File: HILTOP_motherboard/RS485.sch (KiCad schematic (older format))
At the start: 24 parts, among them U13 CME0303S3C, U14 ADuM1401, U15 ADuM1401, U16 CME0303S3C, U17 ISL83491, U18 ISL83491

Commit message: Added new USB2.0 device
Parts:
- removed R72, R78: 0R, Resistors_SMD:R_0603, symbol R
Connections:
- wire segments 124 -> 116
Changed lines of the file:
@@
 LIBS:regul
 LIBS:references
-LIBS:pspice
 LIBS:Power_Management
 LIBS:powerint
@@
 LIBS:Diode
 LIBS:digital-audio
-LIBS:device
 LIBS:Decawave
 LIBS:dc-dc
@@
 LIBS:adc-dac
 LIBS:ac-dc
+LIBS:device
 LIBS:HILTOP_Motherboard-cache
 EELAYER 25 0
@@
 $Descr A4 11693 8268
 encoding utf-8
-Sheet 4 8
+Sheet 4 9
 Title "HILTOP Motherboard"
 Date "26th January 2018"
@@
 F 4 "131-001" H 1950 6700 60  0001 C CNN "Devtank"
 	1    1950 6700
-	1    0    0    -1
-$EndComp
-$Comp
-L GND_ISO3 #PWR0186
-U 1 1 589A9056
-P 3200 7000
-F 0 "#PWR0186" H 3200 6750 50  0001 C CNN
-F 1 "GND_ISO3" H 3200 6850 50  0000 C CNN
-F 2 "" H 3200 7000 50  0000 C CNN
-F 3 "" H 3200 7000 50  0000 C CNN
-	1    3200 7000
 	1    0    0    -1
 $EndComp
@@
 F 3 "" H 5100 1350 50  0000 C CNN
 	1    5100 1350
-	1    0    0    -1
-$EndComp
-$Comp
-L +3V3_ISO3 #PWR0198
-U 1 1 589A906E
-P 3200 6400
-F 0 "#PWR0198" H 3200 6250 50  0001 C CNN
-F 1 "+3V3_ISO3" H 3200 6540 50  0000 C CNN
-F 2 "" H 3200 6400 50  0000 C CNN
-F 3 "" H 3200 6400 50  0000 C CNN
-	1    3200 6400
 	1    0    0    -1
 $EndComp
@@
 	1    0    0    -1
 $EndComp
-$Comp
-L R R78
-U 1 1 589A947C
-P 4450 3250
-F 0 "R78" V 4530 3250 50  0000 C CNN
-F 1 "0R" V 4450 3250 50  0000 C CNN
-F 2 "Resistors_SMD:R_0603" V 4380 3250 50  0001 C CNN
-F 3 "" H 4450 3250 50  0000 C CNN
-F 4 "101-005" V 4450 3250 60  0001 C CNN "Devtank"
-	1    4450 3250
-	0    1    1    0
-$EndComp
 Wire Wire Line
 	6350 1200 6350 1550
@@
 Wire Wire Line
 	3250 3950 3250 4050
-Wire Wire Line
-	4600 3250 5050 3250
-Wire Wire Line
-	5050 3250 5050 2850
-Connection ~ 5050 2850
-Wire Wire Line
-	4300 3250 3900 3250
-Wire Wire Line
-	3900 3250 3900 2850
-Connection ~ 3900 2850
-Wire Wire Line
-	4600 5700 5050 5700
-Wire Wire Line
-	5050 5700 5050 5300
-Connection ~ 5050 5300
-Wire Wire Line
-	4300 5700 3900 5700
-Wire Wire Line
-	3900 5700 3900 5300
-Connection ~ 3900 5300
 $Comp
 L C C108
@@
 $EndComp
 $Comp
-L R R72
-U 1 1 593A9C0A
-P 4450 5700
-F 0 "R72" V 4530 5700 50  0000 C CNN
-F 1 "0R" V 4450 5700 50  0000 C CNN
-F 2 "Resistors_SMD:R_0603" V 4380 5700 50  0001 C CNN
-F 3 "" H 4450 5700 50  0000 C CNN
-F 4 "101-005" V 4450 5700 60  0001 C CNN "Devtank"
-	1    4450 5700
-	0    1    1    0
-$EndComp
-$Comp
 L C C105
 U 1 1 593AA7E2
@@
 Wire Wire Line
 	1050 6850 1050 7050
+$Comp
+L GND_ISO3 #PWR0186
+U 1 1 589A9056
+P 3200 7000
+F 0 "#PWR0186" H 3200 6750 50  0001 C CNN
+F 1 "GND_ISO3" H 3200 6850 50  0000 C CNN
+F 2 "" H 3200 7000 50  0000 C CNN
+F 3 "" H 3200 7000 50  0000 C CNN
+	1    3200 7000
+	1    0    0    -1
+$EndComp
+$Comp
+L +3V3_ISO3 #PWR0198
+U 1 1 589A906E
+P 3200 6400
+F 0 "#PWR0198" H 3200 6250 50  0001 C CNN
+F 1 "+3V3_ISO3" H 3200 6540 50  0000 C CNN
+F 2 "" H 3200 6400 50  0000 C CNN
+F 3 "" H 3200 6400 50  0000 C CNN
+	1    3200 6400
+	1    0    0    -1
+$EndComp
 $EndSCHEMATC

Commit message: Finished CAN nd RS485 interface circuits
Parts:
- removed C105: 4.7uF, Capacitors_SMD:C_0805, symbol C
- removed C108, C84: 100nF, Capacitors_SMD:C_0603, symbol C
- removed C79: 2.2uF, Capacitors_SMD:C_0805, symbol C
- removed JP1, JP2: Jumper_NO_Small, Pin_Headers:Pin_Header_Straight_1x02_Pitch2.54mm, symbol Jumper_NO_Small
- removed L6: 10uH, KiCAD_PCB_Lib:Inductor_MuRata_82103C, symbol L
- removed R80, R81: 100R, Resistors_SMD:R_0603, symbol R
- removed U14, U15: ADuM1401, Housings_SOIC:SOIC-16W_7.5x10.3mm_Pitch1.27mm, symbol ADuM1401
- removed U16: CME0303S3C, KiCAD_PCB_Lib:CME_XXXX_S3C_PSU_MODULE, symbol CME0303S3C
- removed U17, U18: ISL83491, Housings_SOIC:SOIC-14_3.9x8.7mm_Pitch1.27mm, symbol ISL83491
- added C? (x2): 470pF, Capacitor_SMD:C_0603_1608Metric, symbol C
- added C?: 4.7uF, Capacitors_SMD:C_0805, symbol C
- added C?: 2.2uF, Capacitors_SMD:C_0805, symbol C
- added D? (x4): RED_LED, LED_SMD:LED_0603_1608Metric, symbol LED
- added L?: 15uH, KiCAD_PCB_Lib:Inductor_MuRata_82103C, symbol L
- added R? (x4): 10K, Capacitor_SMD:C_0603_1608Metric, symbol R
- added R? (x4): 1K, Capacitor_SMD:C_0603_1608Metric, symbol R
- added U? (x2): ISO3080, Package_SOIC:SOIC-16W_7.5x10.3mm_P1.27mm, symbol ISO3080
- added U? (x4): USB6B1, Housings_SOIC:SOIC-8_3.9x4.9mm_Pitch1.27mm, symbol USB6B1
- added U?: AM1S-0505SZ, KiCAD_PCB_Lib:CME_XXXX_S3C_PSU_MODULE, symbol CME0303S3C
- L5: value 10uH -> 15uH; Devtank 112-004 -> 112-007
- U13: value CME0303S3C -> AM1S-0505SZ; Devtank 131-001 -> 131-002
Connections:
- net labels added: +5V, +5V_ISO3, +5V_ISO4, RS485_CH1_A, RS485_CH1_B, RS485_CH1_RX_LED, RS485_CH1_TX_LED, RS485_CH1_Y, RS485_CH1_Z, RS485_CH2_A, RS485_CH2_B, RS485_CH2_RX_LED, RS485_CH2_TX_LED, RS485_CH2_Y, RS485_CH2_Z
- net labels removed: +3V3_ISO3, +3V3_ISO4, RS485_CH1_AB_IN_+, RS485_CH1_AB_IN_-, RS485_CH1_YZ_OUT_+, RS485_CH1_YZ_OUT_-, RS485_CH2_AB_IN_+, RS485_CH2_AB_IN_-, RS485_CH2_YZ_OUT_+, RS485_CH2_YZ_OUT_-
- wire segments 116 -> 148
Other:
- note removed: "OPTIONAL: Line Termination\n"
- moved on the sheet: C76, C78, C82, C83, L5, U13

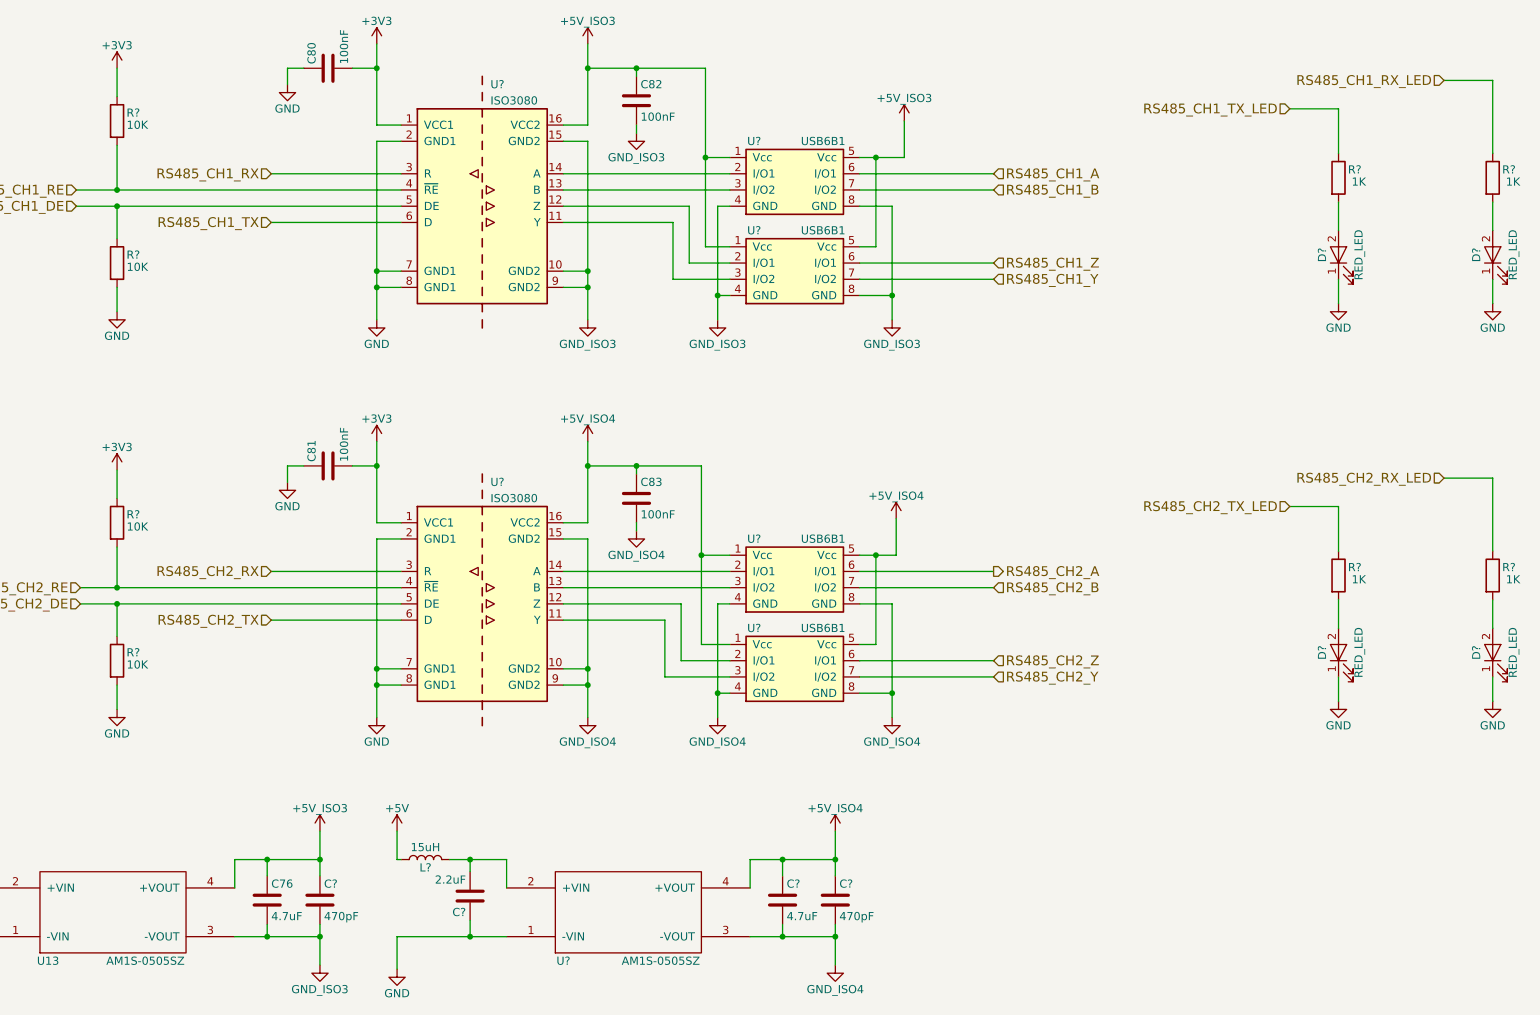
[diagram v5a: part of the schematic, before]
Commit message: Furthe progress on Schematics, assigned all main footprints using latest libraries, removed unwanted tracking and parts from original PCB layout
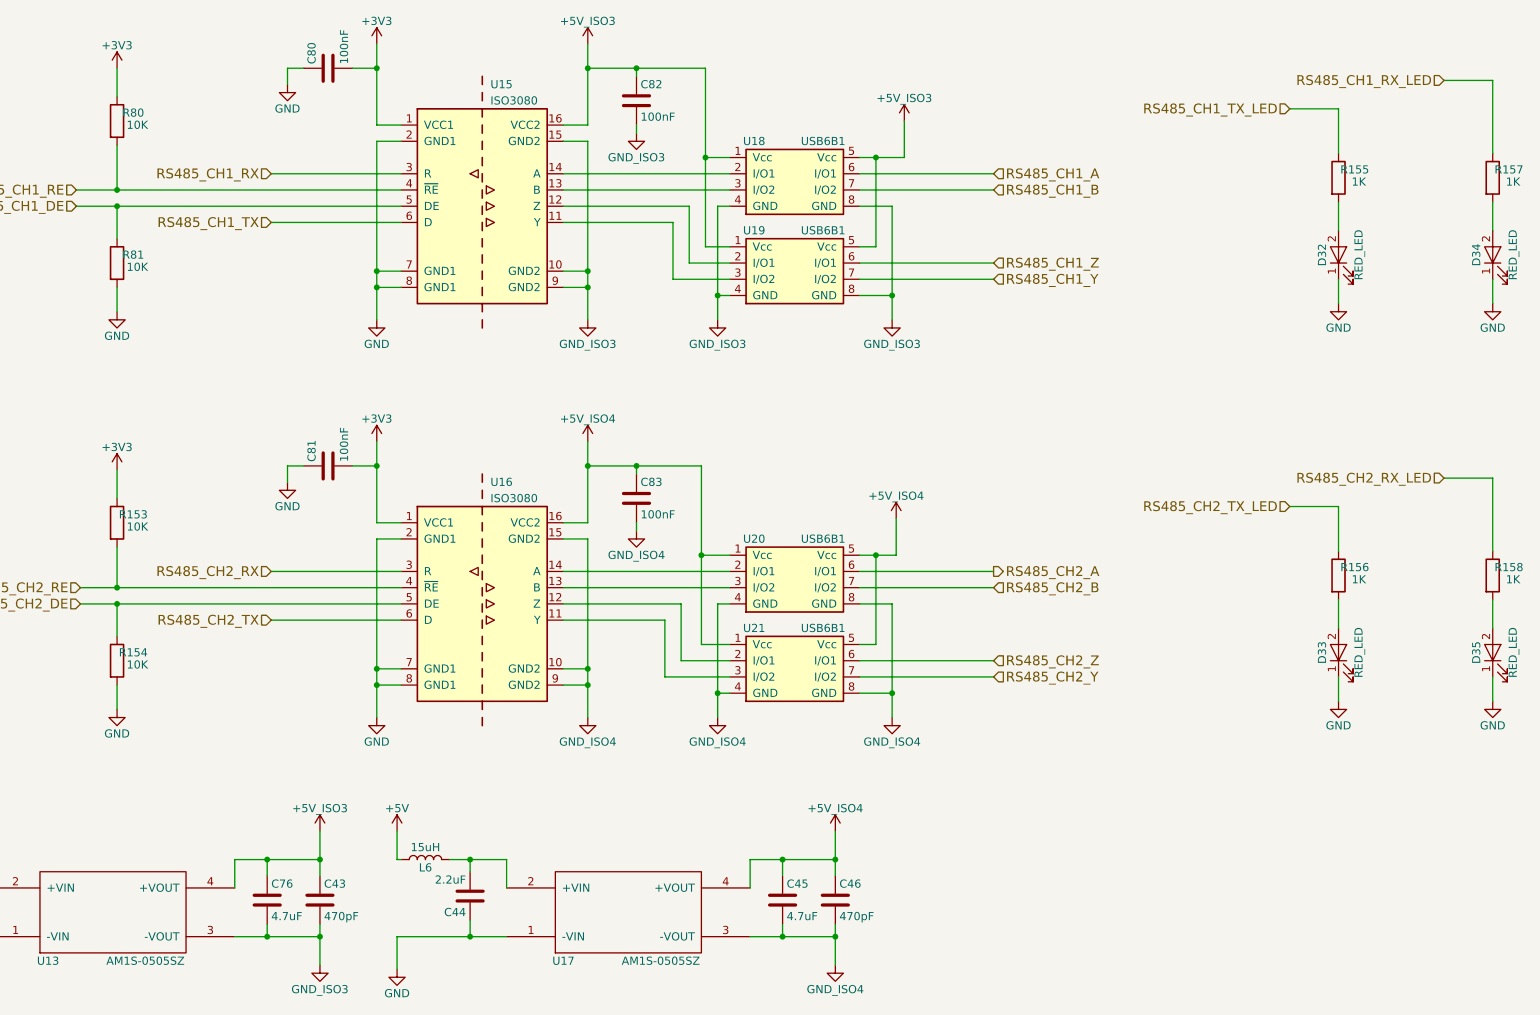
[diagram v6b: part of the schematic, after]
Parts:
- C44, C45: renamed from C?; footprint Capacitors_SMD:C_0805 -> Capacitor_SMD:C_0805_2012Metric
- C76, C78: footprint Capacitors_SMD:C_0805 -> Capacitor_SMD:C_0805_2012Metric
- C80, C81, C82, C83: footprint Capacitors_SMD:C_0603 -> Capacitor_SMD:C_0603_1608Metric
- L5: footprint KiCAD_PCB_Lib:Inductor_MuRata_82103C -> Devtank_PCB_Lib:Inductor_MuRata_82103C
- L6: renamed from L?; footprint KiCAD_PCB_Lib:Inductor_MuRata_82103C -> Devtank_PCB_Lib:Inductor_MuRata_82103C
- R153, R154, R155, R156, R157, R158, R80, R81: renamed from R?; footprint Capacitor_SMD:C_0603_1608Metric -> Resistor_SMD:R_0603_1608Metric
- U13: footprint KiCAD_PCB_Lib:CME_XXXX_S3C_PSU_MODULE -> Devtank_PCB_Lib:CME_XXXX_S3C_PSU_MODULE
- U17: renamed from U?; footprint KiCAD_PCB_Lib:CME_XXXX_S3C_PSU_MODULE -> Devtank_PCB_Lib:CME_XXXX_S3C_PSU_MODULE
- U18, U19, U20, U21: renamed from U?; footprint Housings_SOIC:SOIC-8_3.9x4.9mm_Pitch1.27mm -> Package_SOIC:SOIC-8_3.9x4.9mm_P1.27mm
- gave numbers to parts that had none: 8

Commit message: Schematics complete - 1st draft
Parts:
- removed D32, D33, D34, D35: RED_LED, LED_SMD:LED_0603_1608Metric, symbol LED
- removed R153, R154, R80: 10K, Resistor_SMD:R_0603_1608Metric, symbol R
- removed R155, R156, R157, R158: 1K, Resistor_SMD:R_0603_1608Metric, symbol R
- added C226, C228, C230, C231, C232, C233, C234, C235: 100nF, Capacitor_SMD:C_0603_1608Metric, symbol device:C
- added C227, C229: 1uF, Capacitor_SMD:C_0603_1608Metric, symbol device:C
- added FB10, FB6: 120R_100MHz, Resistor_SMD:R_0603_1608Metric, symbol device:L
- added R221, R222, R244: 10K, Resistor_SMD:R_0603_1608Metric, symbol device:R
- added R223: 0R, Resistor_SMD:R_0603_1608Metric, symbol device:R
- added R243: DNF, Resistor_SMD:R_0603_1608Metric, symbol device:R
- added U43, U44: MAX3107, Package_SO:SSOP-24_5.3x8.2mm_P0.65mm, symbol Devtank:MAX3107
- added Y8, Y9: 3.6864MHz Crystal, Crystal:Crystal_SMD_SeikoEpson_MA505-2Pin_12.7x5.1mm, symbol device:Crystal
- C43, C44, C45, C46, C76, C78, C80, C81, C82, C83: symbol C -> device:C
- L5, L6: symbol L -> device:L
- R81: symbol R -> device:R
- U13, U17: symbol CME0303S3C -> Devtank:CME0303S3C
- U15, U16: symbol ISO3080 -> HILTOP_Motherboard-rescue:ISO3080
- U18, U19, U20, U21: symbol USB6B1 -> ESD_Protection:USB6B1
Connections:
- net RS485_CH1_RE is gone; now on net GND: U15.4 (~RE)
- net RS485_CH2_RE is gone; now on net GND: U16.4 (~RE)
- net +3V3: now also C226.2, C228.2, C232.1, C233.1, C234.1, C235.1, R221.1, R222.1, R243.1, U43.13 (VL), U43.23 (VEXT), U43.5 (~I2C/~SPI), U43.6 (LDOEN), U44.13 (VL), U44.23 (VEXT), U44.5 (~I2C/~SPI), U44.6 (LDOEN)
- net GND: now also C226.1, C227.1, C228.1, C229.1, C230.1, C231.1, C232.2, C233.2, C234.2, C235.2, R244.2, U43.14 (DGND), U43.2 (AGND), U44.14 (DGND), U44.2 (AGND)
- net RS485_CH1_DE: no longer names the net of R81.1, U15.5 (DE)
- net RS485_CH1_DE: now also U43.20 (~RTS~/CLKOUT)
- net RS485_CH1_RX: no longer names the net of U15.3 (R)
- net RS485_CH1_RX: now also U43.21 (RX)
- net RS485_CH1_TX: no longer names the net of U15.6 (D)
- net RS485_CH1_TX: now also U43.22 (TX)
- net RS485_CH2_DE: no longer names the net of U16.5 (DE)
- net RS485_CH2_DE: now also R244.1, U44.20 (~RTS~/CLKOUT)
- net RS485_CH2_RX: no longer names the net of U16.3 (R)
- net RS485_CH2_RX: now also U44.21 (RX)
- net RS485_CH2_TX: no longer names the net of U16.6 (D)
- net RS485_CH2_TX: now also U44.22 (TX)
- new net: U43.1 (XIN), Y8.1
- new net: R223.1, R243.2, U43.12 (~RST), U44.12 (~RST)
- new net: U43.24 (XOUT), Y8.2
- new net: C230.2, FB6.2, U43.3 (VA)
- new net: C227.2, U43.4 (V18)
- new net: U44.1 (XIN), Y9.1
- new net: U44.24 (XOUT), Y9.2
- new net: C231.2, FB10.2, U44.3 (VA)
- new net: C229.2, U44.4 (V18)
- new net +2V5: FB10.1, FB6.1
- new net DIN: U43.10 (DIN/A1), U44.10 (DIN/A1)
- new net DOUT: U43.7 (DOUT/SDA), U44.7 (DOUT/SDA)
- new net SCLK: U43.8 (SCLK/SCL), U44.8 (SCLK/SCL)
- new net UART_CH1_CS: R221.2, U43.9 (~CS/~A0)
- new net UART_CH2_CS: R222.2, U44.9 (~CS/~A0)
- new net UART_IRQ_CH1: U43.11 (~IRQ)
- new net UART_IRQ_CH2: U44.11 (~IRQ)
- new net UART_RESET: R223.2
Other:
- moved on the sheet: C43, C44, C45, C46, C76, C78, C80, C81, C82, C83, L5, L6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

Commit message: BOM nearly complete!
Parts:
- U15, U16: Devtank (none) -> 118-008
- U18, U19, U20, U21: Devtank (none) -> 153-005
- U43, U44: Devtank (none) -> 118-009
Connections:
- no-connect marks 0 -> 11
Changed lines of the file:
@@
 F 2 "Package_SOIC:SOIC-16W_7.5x10.3mm_P1.27mm" H 8275 2275 50  0001 L CIN
 F 3 "" H 8225 3425 50  0000 C CNN
+F 4 "118-008" H 8225 2925 50  0001 C CNN "Devtank"
 	1    8225 2925
 	1    0    0    -1
@@
 F 2 "Package_SOIC:SOIC-16W_7.5x10.3mm_P1.27mm" H 8275 4725 50  0001 L CIN
 F 3 "" H 8225 5875 50  0000 C CNN
+F 4 "118-008" H 8225 5375 50  0001 C CNN "Devtank"
 	1    8225 5375
 	1    0    0    -1
@@
 F 2 "Package_SOIC:SOIC-8_3.9x4.9mm_P1.27mm" H 10125 2425 50  0001 C CNN
 F 3 "" H 10150 2725 50  0001 C CNN
+F 4 "153-005" H 10150 2725 50  0001 C CNN "Devtank"
 	1    10150 2725
 	1    0    0    -1
@@
 F 2 "Package_SOIC:SOIC-8_3.9x4.9mm_P1.27mm" H 10125 2975 50  0001 C CNN
 F 3 "" H 10150 3275 50  0001 C CNN
+F 4 "153-005" H 10150 3275 50  0001 C CNN "Devtank"
 	1    10150 3275
 	1    0    0    -1
@@
 F 2 "Package_SOIC:SOIC-8_3.9x4.9mm_P1.27mm" H 10125 4875 50  0001 C CNN
 F 3 "" H 10150 5175 50  0001 C CNN
+F 4 "153-005" H 10150 5175 50  0001 C CNN "Devtank"
 	1    10150 5175
 	1    0    0    -1
@@
 F 2 "Package_SOIC:SOIC-8_3.9x4.9mm_P1.27mm" H 10125 5425 50  0001 C CNN
 F 3 "" H 10150 5725 50  0001 C CNN
+F 4 "153-005" H 10150 5725 50  0001 C CNN "Devtank"
 	1    10150 5725
 	1    0    0    -1
@@
 F 2 "Package_SO:SSOP-24_5.3x8.2mm_P0.65mm" H 4775 2575 60  0001 C CNN
 F 3 "" H 4775 2575 60  0001 C CNN
+F 4 "118-009" H 4775 2575 50  0001 C CNN "Devtank"
 	1    4775 2575
 	1    0    0    -1
@@
 Wire Wire Line
 	3250 1850 3250 1800
-Wire Wire Line
-	3250 1800 3375 1800
 $Comp
 L device:L FB?
@@
 F 2 "Package_SO:SSOP-24_5.3x8.2mm_P0.65mm" H 4775 5025 60  0001 C CNN
 F 3 "" H 4775 5025 60  0001 C CNN
+F 4 "118-009" H 4775 5025 50  0001 C CNN "Devtank"
 	1    4775 5025
 	1    0    0    -1
@@
 Wire Wire Line
 	1500 5775 1275 5775
+Wire Wire Line
+	3250 1800 3375 1800
+NoConn ~ 5725 3025
+NoConn ~ 5725 3125
+NoConn ~ 5725 3225
+NoConn ~ 5725 3325
+NoConn ~ 5725 3425
+NoConn ~ 5725 5475
+NoConn ~ 5725 5575
+NoConn ~ 5725 5675
+NoConn ~ 5725 5775
+NoConn ~ 5725 5875
+NoConn ~ 18175 2075
 $EndSCHEMATC
